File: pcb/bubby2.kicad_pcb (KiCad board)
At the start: 2 copper layers, 65.1 x 35.2 mm, 7 parts, among them SW0 SW_SPST, SW1 SW_SPST, SW2 SW_SPST, SW3 SW_SPST, SW4 SW_SPST, SW5 SW_DPDT_x2

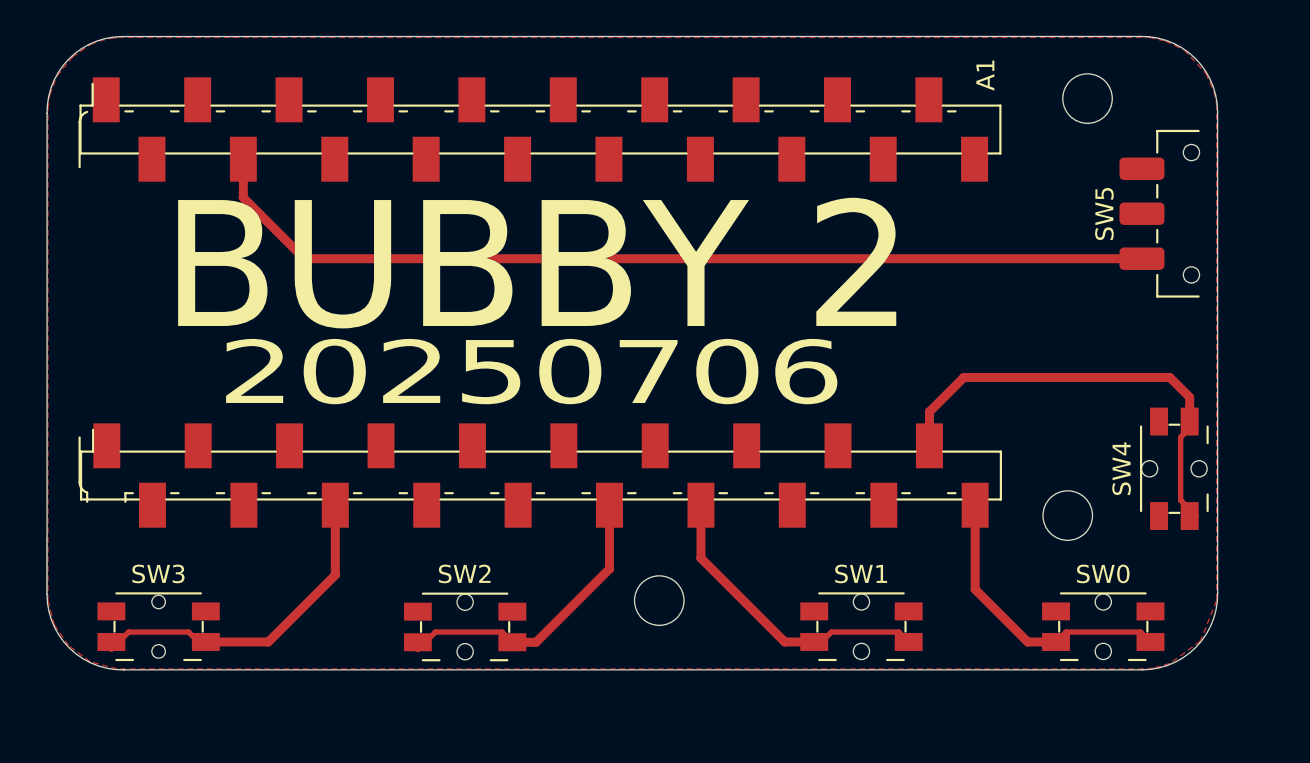
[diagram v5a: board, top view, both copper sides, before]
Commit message: minor fit changes
moved a button, added a screw hole...
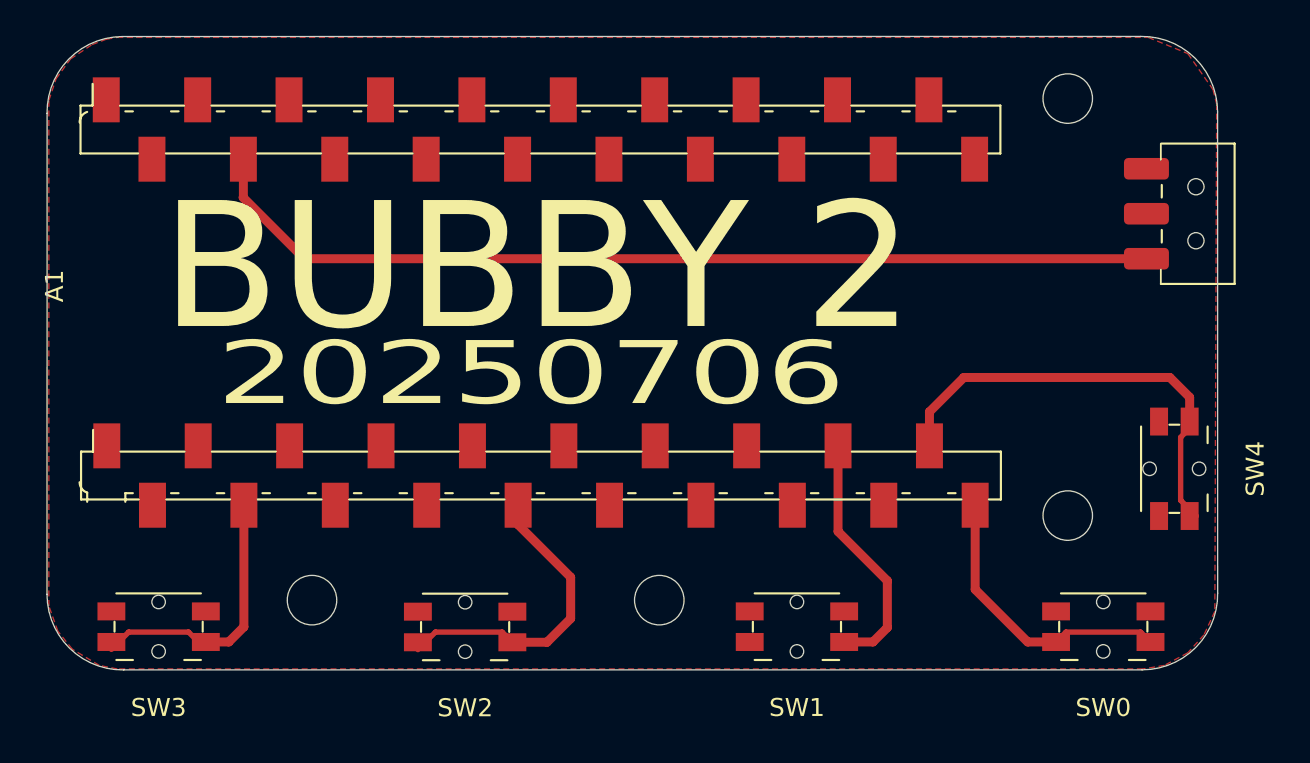
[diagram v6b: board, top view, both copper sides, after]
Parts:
- SW5: footprint footprints:sw_spdt_slide_mskt-12c03 -> sw_spdt_slide_mskt-12c03:Untitled
- moved SW1 3.59 mm to (227.8, 126.5)
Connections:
- A1 pad 10: unconnected-(A1-GPIO7-Pad10) -> Net-(A1-GPIO7)
- A1 pad 12: Net-(A1-GPIO9) -> unconnected-(A1-GPIO9-Pad12)
- A1 pad 14: Net-(A1-GPIO10) -> unconnected-(A1-GPIO10-Pad14)
- A1 pad 17: unconnected-(A1-GPIO13-Pad17) -> Net-(A1-GPIO13)
- A1 pad 4: unconnected-(A1-GPIO2-Pad4) -> Net-(A1-GPIO2)
- A1 pad 6: Net-(A1-GPIO4) -> unconnected-(A1-GPIO4-Pad6)
- SW1 pad 1: Net-(A1-GPIO10) -> Net-(A1-GPIO13)
- SW2 pad 1: Net-(A1-GPIO9) -> Net-(A1-GPIO7)
- SW3 pad 1: Net-(A1-GPIO4) -> Net-(A1-GPIO2)
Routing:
- net Net-(A1-GPIO4): track 17.9 -> 0.00 mm
- net Net-(A1-GPIO7): track 0.00 -> 17.2 mm
- net Net-(A1-GPIO9): track 16.5 -> 0.00 mm
- net Net-(A1-GPIO10): track 16.5 -> 0.00 mm
- net Net-(A1-GPIO2): track 0.00 -> 14.5 mm
- net Net-(A1-GPIO13): track 0.00 -> 14.0 mm
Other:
- outline, holes or cut-outs redrawn

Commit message: good place
* buttons work
* pcb good
* case fit good
* adding in chording code
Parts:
- moved SW4 0.05 mm to (248.7, 117.8)
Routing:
- net Net-(A1-GPIO13): track 14.0 -> 19.7 mm
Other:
- board text added: "20250712"
- board text removed: "20250706"
